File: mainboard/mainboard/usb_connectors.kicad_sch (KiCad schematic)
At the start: 35 parts

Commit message: Fixing labels
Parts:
- gave numbers to parts that had none: 35
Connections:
- net USB_D+ renamed USB.D+
- net USB_D- renamed USB.D-

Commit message: fixed warnings and errors
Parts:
- added C60, C61, C62: (no value), symbol Device:C
- added L3: (no value), symbol Device:L
- F1, F2, F3, F4: value 2A -> (none)
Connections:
- net +5V_VBUS: now also L3.1; no longer C45.1, C46.1, C47.1, C48.1, C51.1, C57.1, F1.2, F2.2, F3.2, F4.2, R19.2, U7.1 (OUT), U8.23 (V5)
- net GND: now also C60.2, C61.2, C62.2
- net VDDA: now also C60.1, C61.1, C62.1, L3.2
- net BUS_RE_USB renamed BUS.RE_USB
- new net +5V_USB_HUB: C45.1, C46.1, C47.1, C48.1, C51.1, C57.1, F1.2, F2.2, F3.2, F4.2, R19.2, U7.1 (OUT), U8.23 (V5)

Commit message: board almost ready, paths must be aligned
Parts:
- removed C41, C42, C43, C44, C53, C55, C56, C57, C58: 100n, symbol Device:C
- removed C45, C46, C47, C48: 100u, symbol Device:C_Polarized
- removed C49, C50: 27p, Capacitor_SMD:C_0402_1005Metric_Pad0.74x0.62mm_HandSolder, symbol Device:C
- removed C51, C52, C54: 10u, symbol Device:C
- removed C60, C61, C62: (no value), symbol Device:C
- removed F1, F2, F3, F4: (no value), symbol Device:Fuse
- removed F5: 2A, symbol Device:Fuse
- removed L3: (no value), symbol Device:L
- removed R13: 4.7k/1%, symbol Device:R
- removed R14: 0, Resistor_SMD:R_0402_1005Metric_Pad0.72x0.64mm_HandSolder, symbol Device:R
- removed R15: 680R/1%, symbol Device:R
- removed R16: 47k, symbol Device:R
- removed R17, R18: 10k, symbol Device:R
- removed R19: 5.1k, symbol Device:R
- removed U7: SY6280, Package_TO_SOT_SMD:SOT-23-5_HandSoldering, symbol project_power:SY6280
- removed U8: GL852, Package_SO:SSOP-28_5.3x10.2mm_P0.65mm, symbol Genesys:GL852
- removed Y2: ABLS-12.000MHZ-B4-T, Crystal:Crystal_SMD_HC49-SD_HandSoldering, symbol Device:Crystal
- added C701, C703: 4.7u, Capacitor_SMD:C_0603_1608Metric_Pad1.08x0.95mm_HandSolder, symbol Device:C
- added C702, C704: 100n, Capacitor_SMD:C_0603_1608Metric_Pad1.08x0.95mm_HandSolder, symbol Device:C
- added F701: 500mA, Fuse:Fuse_1206_3216Metric_Pad1.42x1.75mm_HandSolder, symbol Device:Fuse
- added R701: 100k, Resistor_SMD:R_0603_1608Metric_Pad0.98x0.95mm_HandSolder, symbol Device:R
- added R702: 4.7, Resistor_SMD:R_0603_1608Metric_Pad0.98x0.95mm_HandSolder, symbol Device:R
- added U701: hs8836a, Package_SO:SOP-16_3.9x9.9mm_P1.27mm, symbol HS8836A:hs8836a
- J701: renamed from J13; footprint (none) -> Connector_USB:USB_A_Wuerth_61400826021_Horizontal_Stacked
- J702: renamed from J14; footprint (none) -> Connector_USB:USB_A_Wuerth_61400826021_Horizontal_Stacked
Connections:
- net +5V_USB_HUB: now also J701.1 (VBUS1), J701.5 (VBUS2), J702.1 (VBUS1), J702.5 (VBUS2), F701.2, R702.2
- net +5V_VBUS: now also F701.1
- net D1+: now also J702.3 (D1+), U701.8 (DP1); no longer J701.3 (D1+)
- net D1-: now also J702.2 (D1-), U701.7 (DM1); no longer J701.2 (D1-)
- net D2+: now also J702.7 (D2+), U701.6 (DP2); no longer J701.7 (D2+)
- net D2-: now also J702.6 (D2-), U701.5 (DM2); no longer J701.6 (D2-)
- net D3+: now also J701.3 (D1+), U701.4 (DP3); no longer J702.3 (D1+)
- net D3-: now also J701.2 (D1-), U701.3 (DM3); no longer J702.2 (D1-)
- net D4+: now also J701.7 (D2+), U701.2 (DP4); no longer J702.7 (D2+)
- net D4-: now also J701.6 (D2-), U701.1 (DM4); no longer J702.6 (D2-)
- net GND: now also C701.2, C702.2, C703.2, C704.2, R701.1, U701.16 (GND)
- net USB.D+: now also U701.10 (DM)
- net USB.D-: now also U701.11 (DP)
- new net: C703.1, C704.1, R702.1, U701.13 (VCC)
- new net: R701.2, U701.9 (REF)
- new net +3V3_USB_HUB: C701.1, C702.1, U701.12 (DCP), U701.14 (V33)
- no-connect marks 3 -> 1

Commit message: motherboard designed
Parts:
- U: renamed from F701; value 500mA -> (none); footprint Fuse:Fuse_1206_3216Metric_Pad1.42x1.75mm_HandSolder -> (none)
- U: renamed from C704; value 100n -> (none); footprint Capacitor_SMD:C_0603_1608Metric_Pad1.08x0.95mm_HandSolder -> (none)
- U: renamed from J701; value ~ -> (none); footprint Connector_USB:USB_A_Wuerth_61400826021_Horizontal_Stacked -> (none)
- U: renamed from R701; value 100k -> (none); footprint Resistor_SMD:R_0603_1608Metric_Pad0.98x0.95mm_HandSolder -> (none)
- U: renamed from C703; value 4.7u -> (none); footprint Capacitor_SMD:C_0603_1608Metric_Pad1.08x0.95mm_HandSolder -> (none)
- U: renamed from U701; value hs8836a -> (none); footprint Package_SO:SOP-16_3.9x9.9mm_P1.27mm -> (none)
- U: renamed from J702; value ~ -> (none); footprint Connector_USB:USB_A_Wuerth_61400826021_Horizontal_Stacked -> (none)
- U: renamed from C702; value 100n -> (none); footprint Capacitor_SMD:C_0603_1608Metric_Pad1.08x0.95mm_HandSolder -> (none)
- U: renamed from C701; value 4.7u -> (none); footprint Capacitor_SMD:C_0603_1608Metric_Pad1.08x0.95mm_HandSolder -> (none)
- U: renamed from R702; value 4.7 -> (none); footprint Resistor_SMD:R_0603_1608Metric_Pad0.98x0.95mm_HandSolder -> (none)

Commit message: schematic for gpu extension
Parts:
- C701, C703: renamed from U; value (none) -> 4.7u; footprint (none) -> Capacitor_SMD:C_0603_1608Metric_Pad1.08x0.95mm_HandSolder
- C702, C704: renamed from U; value (none) -> 100n; footprint (none) -> Capacitor_SMD:C_0603_1608Metric_Pad1.08x0.95mm_HandSolder
- F701: renamed from U; value (none) -> 500mA; footprint (none) -> Fuse:Fuse_1206_3216Metric_Pad1.42x1.75mm_HandSolder
- J701, J702: renamed from U; value (none) -> ~; footprint (none) -> Connector_USB:USB_A_Wuerth_61400826021_Horizontal_Stacked
- R701: renamed from U; value (none) -> 100k; footprint (none) -> Resistor_SMD:R_0603_1608Metric_Pad0.98x0.95mm_HandSolder
- R702: renamed from U; value (none) -> 4.7; footprint (none) -> Resistor_SMD:R_0603_1608Metric_Pad0.98x0.95mm_HandSolder
- U701: renamed from U; value (none) -> hs8836a; footprint (none) -> Package_SO:SOP-16_3.9x9.9mm_P1.27mm

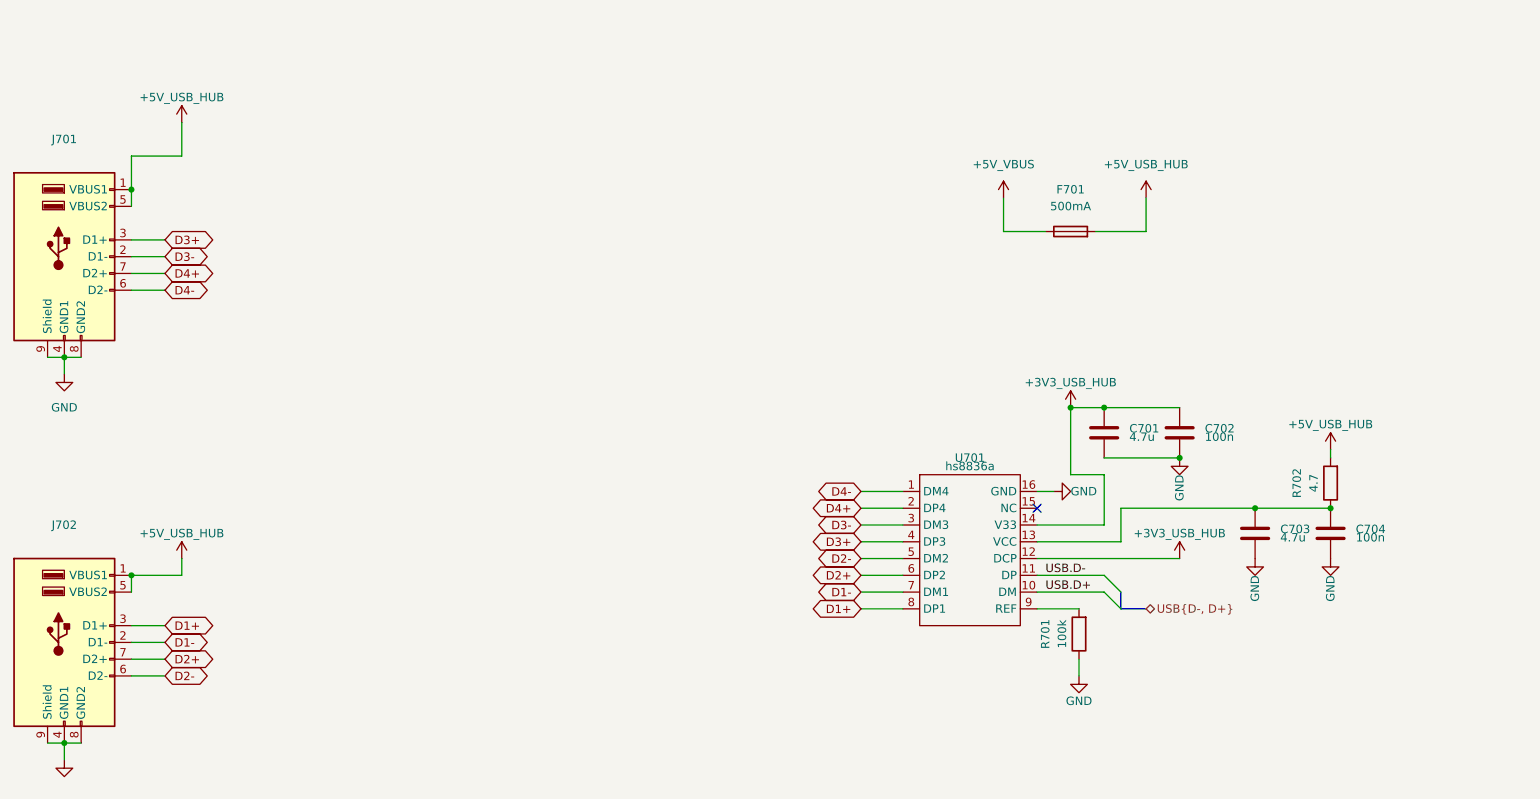
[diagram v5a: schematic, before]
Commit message: some ERC fixes
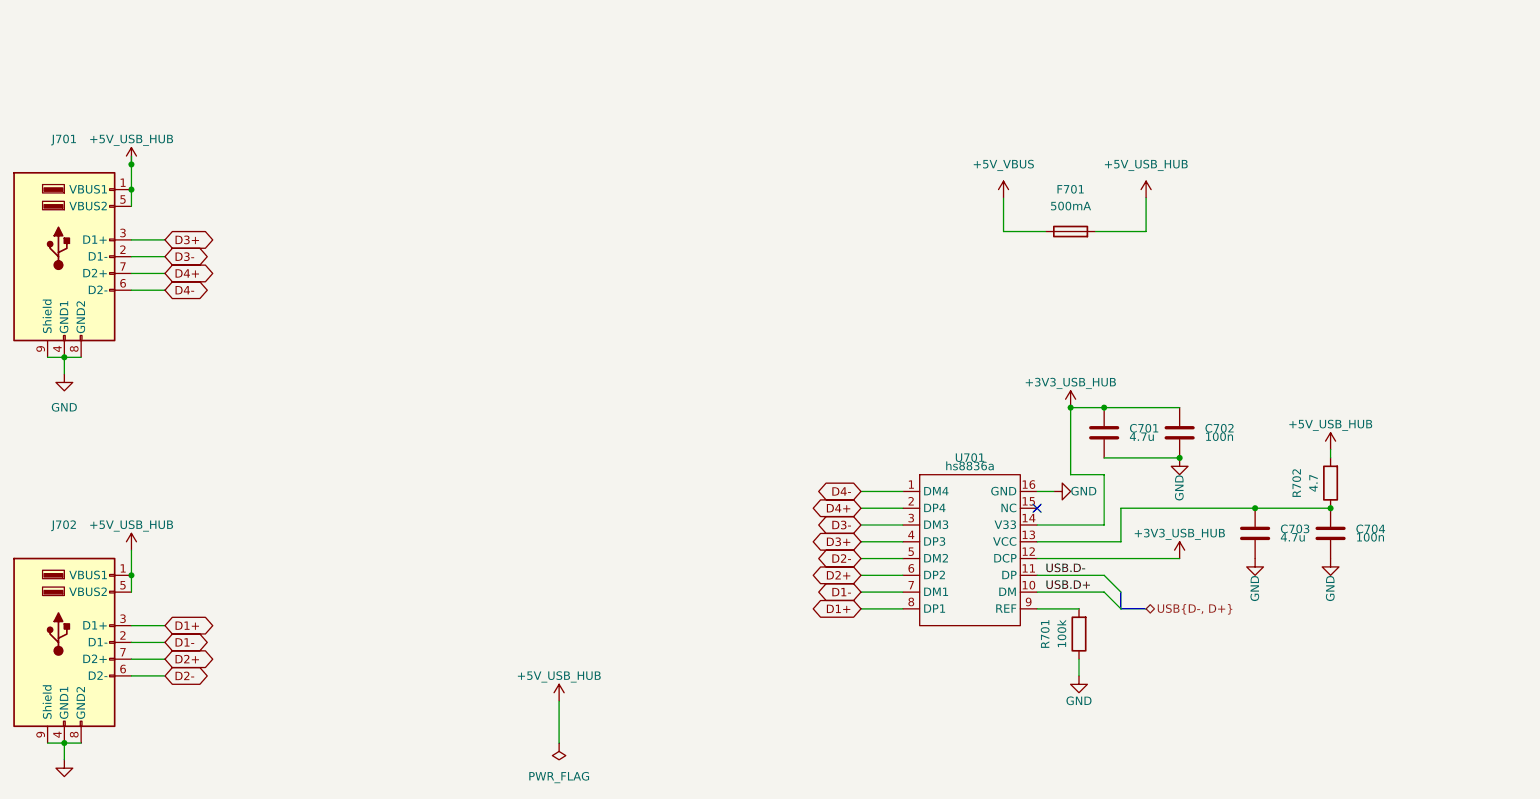
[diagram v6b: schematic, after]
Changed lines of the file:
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@@
   (junction (at 219.71 88.9) (diameter 0) (color 0 0 0 0)
+  )
+  (junction (at 60.96 44.45) (diameter 0) (color 0 0 0 0)
   )
   (junction (at 60.96 106.68) (diameter 0) (color 0 0 0 0)
@@
     (stroke (width 0) (type default))
   )
-  (wire (pts (xy 60.96 106.68) (xy 68.58 106.68))
-    (stroke (width 0) (type default))
-  )
   (wire (pts (xy 50.8 132.08) (xy 50.8 134.62))
     (stroke (width 0) (type default))
@@
     (stroke (width 0) (type default))
   )
-  (wire (pts (xy 68.58 38.1) (xy 68.58 43.18))
-    (stroke (width 0) (type default))
-  )
   (wire (pts (xy 60.96 50.8) (xy 60.96 48.26))
     (stroke (width 0) (type default))
@@
     (stroke (width 0) (type default))
   )
-  (wire (pts (xy 68.58 104.14) (xy 68.58 106.68))
+  (wire (pts (xy 60.96 102.87) (xy 60.96 106.68))
     (stroke (width 0) (type default))
   )
@@
     (stroke (width 0) (type default))
   )
-  (wire (pts (xy 210.82 101.6) (xy 198.12 101.6))
-    (stroke (width 0) (type default))
-  )
   (wire (pts (xy 171.45 111.76) (xy 177.8 111.76))
     (stroke (width 0) (type default))
@@
     (stroke (width 0) (type default))
   )
-  (wire (pts (xy 60.96 48.26) (xy 60.96 43.18))
+  (wire (pts (xy 60.96 48.26) (xy 60.96 44.45))
     (stroke (width 0) (type default))
   )
@@
     (stroke (width 0) (type default))
   )
+  (wire (pts (xy 198.12 101.6) (xy 210.82 101.6))
+    (stroke (width 0) (type default))
+  )
+  (wire (pts (xy 125.73 125.73) (xy 125.73 132.08))
+    (stroke (width 0) (type default))
+  )
   (wire (pts (xy 60.96 121.92) (xy 66.04 121.92))
     (stroke (width 0) (type default))
@@
     (stroke (width 0) (type default))
   )
-  (wire (pts (xy 60.96 43.18) (xy 68.58 43.18))
+  (wire (pts (xy 60.96 44.45) (xy 60.96 43.18))
     (stroke (width 0) (type default))
   )
@@
     )
   )
-  (symbol (lib_name "+3V3_USB_HUB_1") (lib_id "project_power:+3V3_USB_HUB") (at 219.71 104.14 0) (unit 1)
+  (symbol (lib_id "project_power:+3V3_USB_HUB") (at 219.71 104.14 0) (unit 1)
     (in_bom yes) (on_board yes) (dnp no)
     (property "Reference" "#PWR0711" (at 219.71 107.95 0)
@@
   (symbol (lib_id "project_power:+5V_USB_HUB") (at 242.57 87.63 0) (unit 1)
     (in_bom yes) (on_board yes) (dnp no)
-    (property "Reference" "#PWR0713" (at 242.57 91.44 0)
+    (property "Reference" "#PWR0155" (at 248.92 90.17 0)
       (effects (font (size 1.27 1.27)) hide)
     )
@@
       (project "mainboard"
         (path "/e63e39d7-6ac0-4ffd-8aa3-1841a4541b55/b04c7282-7715-4444-b680-e16531d85cc8"
-          (reference "#PWR0713") (unit 1) (value "+5V_USB_HUB") (footprint "")
+          (reference "#PWR0155") (unit 1) (value "+5V_USB_HUB") (footprint "")
+        )
+      )
+    )
+  )
+  (symbol (lib_id "power:PWR_FLAG") (at 125.73 132.08 180) (unit 1)
+    (in_bom yes) (on_board yes) (dnp no) (fields_autoplaced)
+    (property "Reference" "#FLG0103" (at 125.73 133.985 0)
+      (effects (font (size 1.27 1.27)) hide)
+    )
+    (property "Value" "PWR_FLAG" (at 125.73 137.16 0)
+      (effects (font (size 1.27 1.27)))
+    )
+    (property "Footprint" "" (at 125.73 132.08 0)
+      (effects (font (size 1.27 1.27)) hide)
+    )
+    (property "Datasheet" "~" (at 125.73 132.08 0)
+      (effects (font (size 1.27 1.27)) hide)
+    )
+    (pin "1")
+    (instances
+      (project "mainboard"
+        (path "/e63e39d7-6ac0-4ffd-8aa3-1841a4541b55/b04c7282-7715-4444-b680-e16531d85cc8"
+          (reference "#FLG0103") (unit 1) (value "PWR_FLAG") (footprint "")
         )
       )
@@
     )
   )
-  (symbol (lib_name "+3V3_USB_HUB_1") (lib_id "project_power:+3V3_USB_HUB") (at 203.2 81.28 0) (unit 1)
-    (in_bom yes) (on_board yes) (dnp no)
-    (property "Reference" "#PWR0707" (at 203.2 85.09 0)
+  (symbol (lib_id "project_power:+3V3_USB_HUB") (at 203.2 81.28 0) (unit 1)
+    (in_bom yes) (on_board yes) (dnp no)
+    (property "Reference" "#PWR0156" (at 203.2 85.09 0)
       (effects (font (size 1.27 1.27)) hide)
     )
@@
       (project "mainboard"
         (path "/e63e39d7-6ac0-4ffd-8aa3-1841a4541b55/b04c7282-7715-4444-b680-e16531d85cc8"
-          (reference "#PWR0707") (unit 1) (value "+3V3_USB_HUB") (footprint "")
+          (reference "#PWR0156") (unit 1) (value "+3V3_USB_HUB") (footprint "")
+        )
+      )
+    )
+  )
+  (symbol (lib_id "project_power:+5V_USB_HUB") (at 125.73 125.73 0) (unit 1)
+    (in_bom yes) (on_board yes) (dnp no)
+    (property "Reference" "#PWR0713" (at 125.73 129.54 0)
+      (effects (font (size 1.27 1.27)) hide)
+    )
+    (property "Value" "+5V_USB_HUB" (at 125.73 121.92 0)
+      (effects (font (size 1.27 1.27)))
+    )
+    (property "Footprint" "" (at 125.73 125.73 0)
+      (effects (font (size 1.27 1.27)) hide)
+    )
+    (property "Datasheet" "" (at 125.73 125.73 0)
+      (effects (font (size 1.27 1.27)) hide)
+    )
+    (pin "1")
+    (instances
+      (project "mainboard"
+        (path "/e63e39d7-6ac0-4ffd-8aa3-1841a4541b55/b04c7282-7715-4444-b680-e16531d85cc8"
+          (reference "#PWR0713") (unit 1) (value "+5V_USB_HUB") (footprint "")
         )
       )
@@
     )
   )
-  (symbol (lib_id "project_power:+5V_USB_HUB") (at 68.58 104.14 0) (unit 1)
-    (in_bom yes) (on_board yes) (dnp no)
-    (property "Reference" "#PWR0704" (at 68.58 107.95 0)
-      (effects (font (size 1.27 1.27)) hide)
-    )
-    (property "Value" "+5V_USB_HUB" (at 68.58 100.33 0)
-      (effects (font (size 1.27 1.27)))
-    )
-    (property "Footprint" "" (at 68.58 104.14 0)
-      (effects (font (size 1.27 1.27)) hide)
-    )
-    (property "Datasheet" "" (at 68.58 104.14 0)
+  (symbol (lib_id "project_power:+5V_USB_HUB") (at 60.96 102.87 0) (unit 1)
+    (in_bom yes) (on_board yes) (dnp no)
+    (property "Reference" "#PWR0704" (at 60.96 106.68 0)
+      (effects (font (size 1.27 1.27)) hide)
+    )
+    (property "Value" "+5V_USB_HUB" (at 60.96 99.06 0)
+      (effects (font (size 1.27 1.27)))
+    )
+    (property "Footprint" "" (at 60.96 102.87 0)
+      (effects (font (size 1.27 1.27)) hide)
+    )
+    (property "Datasheet" "" (at 60.96 102.87 0)
       (effects (font (size 1.27 1.27)) hide)
     )
@@
     )
   )
-  (symbol (lib_id "project_power:+5V_USB_HUB") (at 68.58 38.1 0) (unit 1)
-    (in_bom yes) (on_board yes) (dnp no)
-    (property "Reference" "#PWR0703" (at 68.58 41.91 0)
-      (effects (font (size 1.27 1.27)) hide)
-    )
-    (property "Value" "+5V_USB_HUB" (at 68.58 34.29 0)
-      (effects (font (size 1.27 1.27)))
-    )
-    (property "Footprint" "" (at 68.58 38.1 0)
-      (effects (font (size 1.27 1.27)) hide)
-    )
-    (property "Datasheet" "" (at 68.58 38.1 0)
-      (effects (font (size 1.27 1.27)) hide)
-    )
+  (symbol (lib_id "project_power:+5V_USB_HUB") (at 60.96 44.45 0) (unit 1)
+    (in_bom yes) (on_board yes) (dnp no)
+    (property "Reference" "#PWR0703" (at 60.96 48.26 0)
+      (effects (font (size 1.27 1.27)) hide)
+    )
+    (property "Value" "+5V_USB_HUB" (at 60.96 40.64 0)
+      (effects (font (size 1.27 1.27)))
+    )
+    (property "Footprint" "" (at 60.96 44.45 0)
+      (effects (font (size 1.27 1.27)) hide)
+    )
+    (property "Datasheet" "" (at 60.96 44.45 0)
+      (effects (font (size 1.27 1.27)) hide)
+    )
